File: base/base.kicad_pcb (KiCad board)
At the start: 2 copper layers, 100 x 100 mm, 108 parts, among them J1 Screw_Terminal_01x02, J2 Out, Q1 MSB92W, Q2 MJD31C, Q3 IPD50R3K0CE, Q4 MJD31C, Q5 MMBTA42, Q6 MMBTA42, Q7 MMBTA42, Q8 MMBTA42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

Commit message: Backup
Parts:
- D2: footprint Diode_THT:D_DO-41_SOD81_P10.16mm_Horizontal -> Diode_SMD:D_SMB
- moved C12 20.3 mm to (137.0, 112.0), turned to 180 degrees
- moved C20 13.7 mm to (144.9, 112.0), turned to 180 degrees
- moved R27 10.4 mm to (65.3, 121.9), turned to 45 degrees
- moved R26 8.75 mm to (68.0, 118.9), turned to 45 degrees
- moved C6 8.56 mm to (67.3, 123.9), turned to 225 degrees
- moved C18 7.86 mm to (70.3, 116.9), turned to 315 degrees
- moved D8 7.61 mm to (86.1, 99.8), turned to 90 degrees
- moved C16 6.87 mm to (69.3, 125.9), turned to 225 degrees
- moved R23 6.77 mm to (127.0, 120.5), turned to 245 degrees
- moved Q5 6.66 mm to (81.8, 99.6), turned to 180 degrees
- moved U3 6.56 mm to (70.3, 121.3), turned to 45 degrees
- moved R31 6.51 mm to (87.9, 104.4), turned to 180 degrees
- moved D9 6.49 mm to (88.4, 107.9), turned to 180 degrees
- moved C7 5.66 mm to (73.3, 118.5), turned to 45 degrees
- moved C19 5.43 mm to (71.4, 127.9), turned to 45 degrees
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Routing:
- net Net-(C17-Pad1): track 0.00 -> 67.4 mm
- net GND: track 0.00 -> 53.6 mm
- net -HV: track 0.00 -> 35.1 mm
- net Net-(C21-Pad1): track 0.00 -> 32.1 mm, vias 0 -> 2
- net Net-(C20-Pad1): track 0.00 -> 30.5 mm
- net Net-(C22-Pad1): track 0.00 -> 26.7 mm, vias 0 -> 2
- net Net-(C23-Pad1): track 0.00 -> 25.6 mm, vias 0 -> 2
- net Net-(PMT1-Pad13): track 0.00 -> 22.0 mm
- net Net-(C24-Pad1): track 0.00 -> 21.0 mm, vias 0 -> 1
- net Net-(D11-Pad1): track 0.00 -> 18.9 mm
- net Net-(D4-Pad1): track 0.00 -> 18.4 mm
- net Net-(L1-Pad1): track 0.00 -> 17.9 mm
- net Net-(PMT1-Pad6): track 0.00 -> 17.7 mm
- net Net-(Q4-Pad1): track 0.00 -> 13.4 mm
- net Net-(C25-Pad1): track 0.00 -> 13.3 mm
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
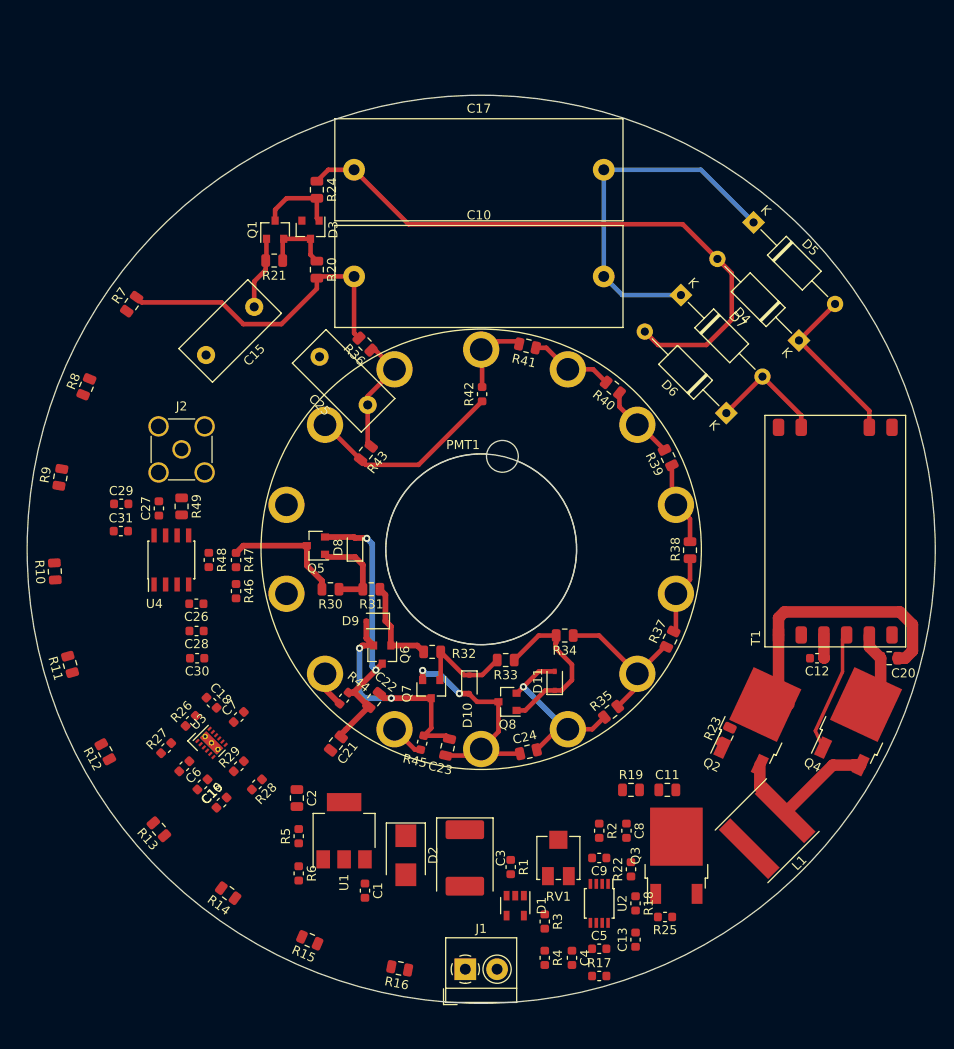
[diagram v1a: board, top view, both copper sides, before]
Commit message: Added optional G23736 (electronic goldmine) footprint
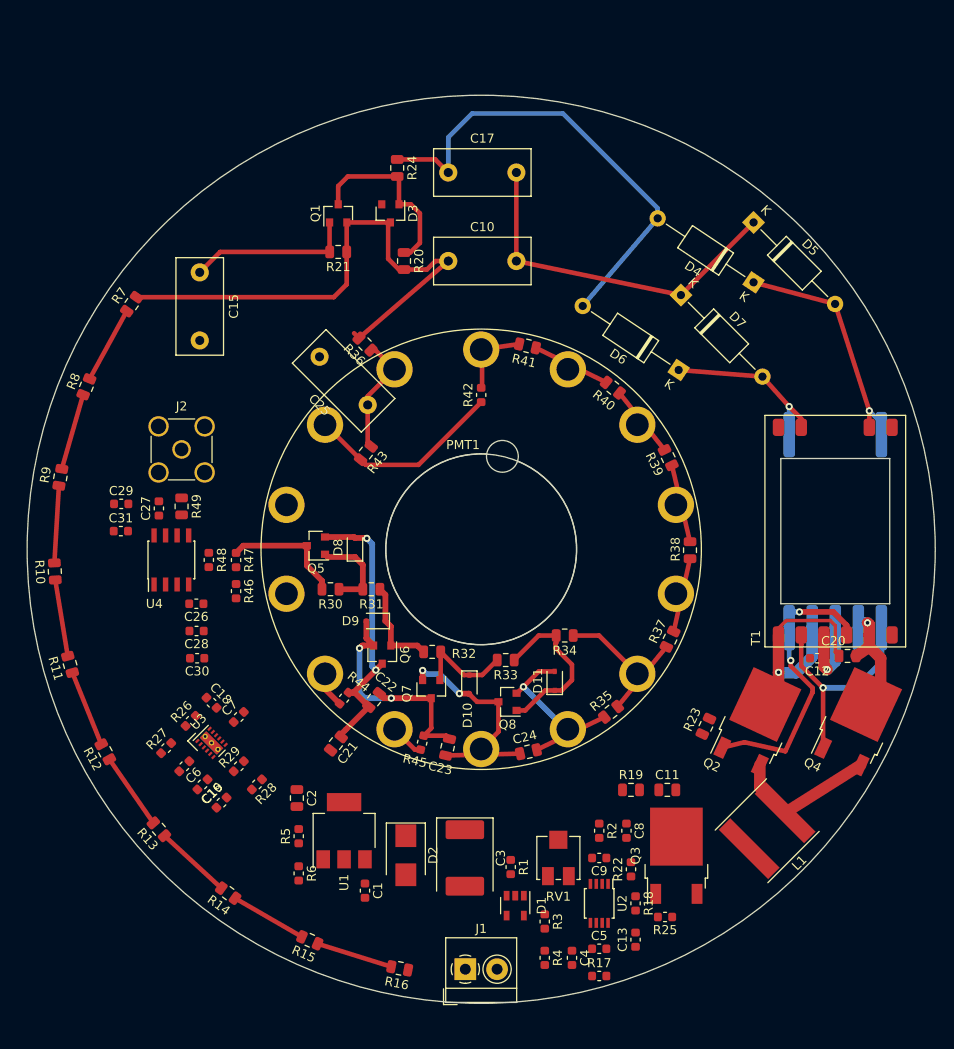
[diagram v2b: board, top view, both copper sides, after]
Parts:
- added TT1: FL2015-3LB, FL2015-3LB:G23736, F.Cu at (139.0, 98.0)
- C10: value 15n -> 10n; footprint Capacitor_THT:C_Rect_L31.5mm_W11.0mm_P27.50mm_MKS4 -> Capacitor_THT:C_Disc_D10.5mm_W5.0mm_P7.50mm
- C17: value 33n -> 10n; footprint Capacitor_THT:C_Rect_L31.5mm_W11.0mm_P27.50mm_MKS4 -> Capacitor_THT:C_Disc_D10.5mm_W5.0mm_P7.50mm
- R20: value 10k -> 0
- moved C10 10.5 mm to (96.4, 68.2)
- moved C17 10.4 mm to (96.4, 58.5)
- moved R20 9.65 mm to (91.5, 68.2)
- moved R24 9.17 mm to (90.8, 58.0)
- moved D3 8.98 mm to (90.0, 63.0)
- moved D4 8.12 mm to (130.0, 70.6), turned to 146.3 degrees
- moved Q1 7.18 mm to (84.2, 63.0)
- moved R21 7.11 mm to (84.2, 67.2)
- moved C15 7.10 mm to (69.0, 69.5), turned to 270 degrees
- moved D6 7.08 mm to (121.8, 80.2), turned to 146.3 degrees
- moved C20 4.59 mm to (140.3, 111.8), turned to 0 degrees
- moved R23 2.46 mm to (124.8, 119.5)
- moved R42 0.13 mm to (100.0, 83.0)
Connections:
- D3 pad 1: Net-(D3-Pad1) -> -HV
- Q1 pad 2: Net-(D3-Pad1) -> -HV
- R20 pad 1: Net-(D3-Pad1) -> Net-(D3-Pad2)
- R21 pad 1: Net-(D3-Pad1) -> -HV
- T1 pad 2: Net-(Q2-Pad1) -> Net-(Q4-Pad1)
- T1 pad 4: Net-(Q4-Pad1) -> Net-(Q2-Pad1)
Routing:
- net Net-(Q2-Pad1): track 0.00 -> 32.8 mm, vias 0 -> 2
- net -HV: track 35.1 -> 60.7 mm
- net Net-(C17-Pad1): track 67.4 -> 52.4 mm
- net Net-(Q4-Pad1): track 13.4 -> 24.8 mm, vias 0 -> 1
- net Net-(D3-Pad2): track 8.89 -> 20.2 mm
- net Net-(C15-Pad1): track 8.06 -> 18.5 mm
- net Net-(R13-Pad1): track 0.00 -> 8.51 mm
- net Net-(R15-Pad1): track 0.00 -> 8.51 mm
- net Net-(R8-Pad2): track 0.00 -> 8.51 mm
- net Net-(R11-Pad1): track 0.00 -> 8.51 mm
- net Net-(R10-Pad1): track 0.00 -> 8.51 mm
- net Net-(R12-Pad2): track 0.00 -> 8.51 mm
- net Net-(R10-Pad2): track 0.00 -> 8.51 mm
- net Net-(R7-Pad1): track 0.00 -> 8.51 mm
- net Net-(R14-Pad2): track 0.00 -> 8.51 mm
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
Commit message: More routing. Removed excessive ripper remover
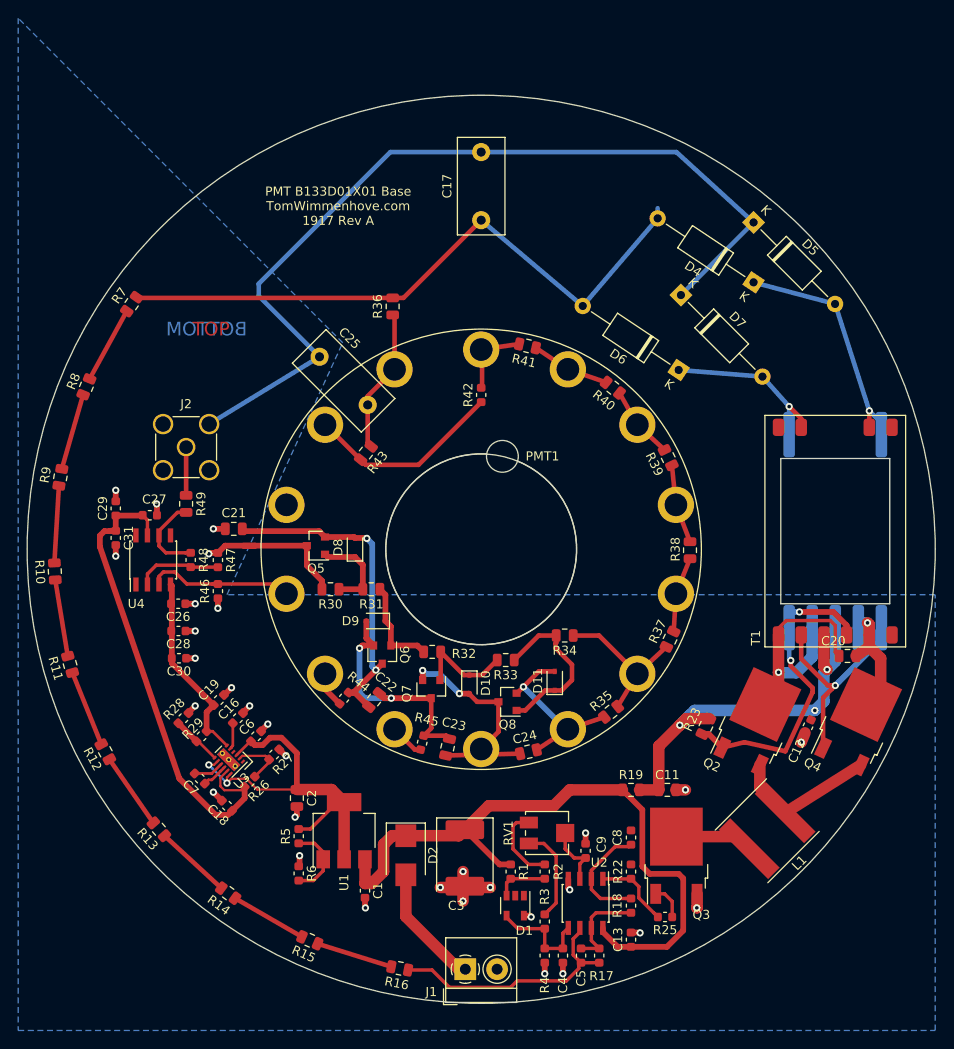
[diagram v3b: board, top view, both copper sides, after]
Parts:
- removed C10, C15: 10n, Capacitor_THT:C_Disc_D10.5mm_W5.0mm_P7.50mm
- removed D3: BZX84C47, Diode_SMD:D_SOT-23_ANK
- removed Q1: MSB92W, Package_TO_SOT_SMD:SOT-23
- removed R20: 0, Resistor_SMD:R_0805_2012Metric
- removed R21: 10M, Resistor_SMD:R_0805_2012Metric
- removed R24: 10k, Resistor_SMD:R_0805_2012Metric
- U2: footprint Package_SO:TSSOP-8_3x3mm_P0.65mm -> Package_SO:SOIC-8_3.9x4.9mm_P1.27mm
- moved C21 26.2 mm to (72.8, 97.8), turned to 180 degrees
- moved R27 11.9 mm to (77.2, 122.6), turned to 225 degrees
- moved C18 11.5 mm to (72.0, 128.2), turned to 135 degrees
- moved C19 11.3 mm to (71.1, 116.6), turned to 225 degrees
- moved R28 10.9 mm to (67.2, 118.6), turned to 45 degrees
- moved R26 9.33 mm to (74.5, 125.6), turned to 225 degrees
- moved C6 8.56 mm to (75.2, 120.6), turned to 45 degrees
- moved C16 8.28 mm to (73.2, 118.6), turned to 45 degrees
- moved C7 8.02 mm to (69.0, 125.2), turned to 135 degrees
- moved C12 7.57 mm to (136.0, 119.5), turned to 245 degrees
- moved R2 7.50 mm to (107.0, 135.5), turned to 90 degrees
- moved C17 6.38 mm to (100.0, 63.8), turned to 90 degrees
- moved R29 5.26 mm to (69.2, 120.6), turned to 225 degrees
- moved R36 5.15 mm to (90.2, 73.2), turned to 90 degrees
- moved RV1 3.02 mm to (107.2, 131.2), turned to 90 degrees
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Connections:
- C17 pad 1: Net-(C17-Pad1) -> -HV
- D4 pad 2: Net-(C17-Pad1) -> -HV
- D6 pad 2: Net-(C17-Pad1) -> -HV
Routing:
- net GND: track 53.2 -> 156.9 mm, vias 0 -> 31
- net +12V: track 0.00 -> 74.5 mm
- net +5V: track 0.00 -> 53.2 mm
- net Net-(C17-Pad1): track 52.4 -> 0.00 mm
- net Net-(C2-Pad1): track 0.00 -> 44.4 mm, vias 0 -> 2
- net Net-(C11-Pad1): track 8.95 -> 43.3 mm, vias 1 -> 3
- net Net-(C5-Pad1): track 0.00 -> 27.7 mm
- net -5V: track 0.00 -> 21.4 mm
- net Net-(D3-Pad2): track 20.2 -> 0.00 mm
- net Net-(C15-Pad1): track 18.5 -> 0.00 mm
- net Net-(PMT1-Pad11): track 0.00 -> 16.2 mm
- net Net-(D2-Pad2): track 0.00 -> 13.6 mm
- net Net-(C8-Pad2): track 0.00 -> 12.4 mm
- net Net-(C4-Pad1): track 0.00 -> 11.6 mm
- net Net-(R3-Pad1): track 0.00 -> 10.5 mm
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- added copper zone on B.Cu, net GND
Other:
- board text added: "BOTTOM"
- board text added: "PMT B133D01X01 Base TomWimmenhove.com 1917 Rev A"
- board text added: "TOP"

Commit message: Moved stuff around. Added isolation slots.
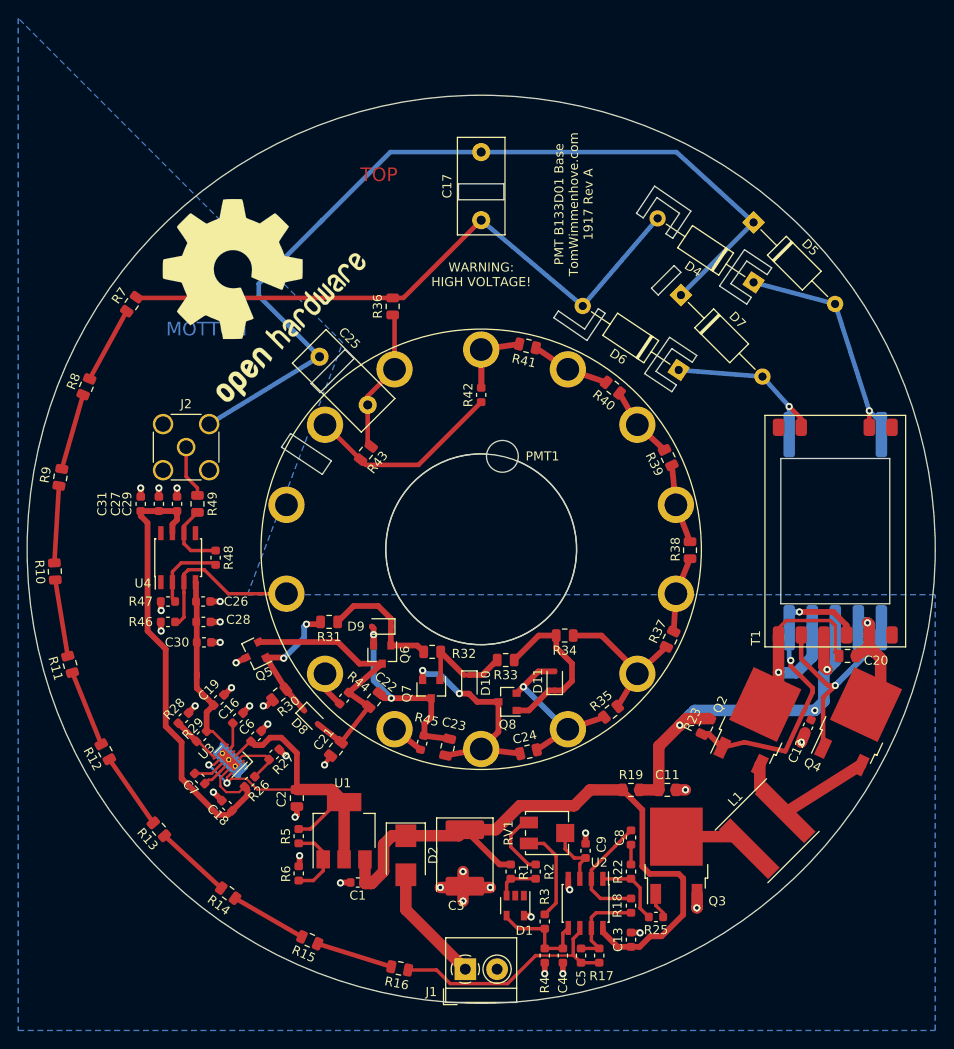
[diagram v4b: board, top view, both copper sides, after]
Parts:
- added REF**: OSHW-Logo2_24.3x20mm_SilkScreen, Symbol:OSHW-Logo2_24.3x20mm_SilkScreen, F.Cu at (73.8, 70.2)
- J2: footprint Connector_Coaxial:SMA_Amphenol_901-144_Vertical -> Connector_Coaxial:SMA_Amphenol_132291-12_Vertical
- moved C21 26.7 mm to (84.0, 122.0), turned to 231.4 degrees
- moved D8 19.3 mm to (81.2, 118.5), turned to 315 degrees
- moved Q5 13.7 mm to (75.0, 111.5), turned to 205.7 degrees
- moved R30 12.9 mm to (77.8, 116.0), turned to 218.6 degrees
- moved R47 7.15 mm to (65.5, 105.8), turned to 0 degrees
- moved C29 6.77 mm to (66.5, 95.0)
- moved R46 6.46 mm to (65.5, 108.0), turned to 0 degrees
- moved R31 5.88 mm to (83.2, 108.0)
- moved C31 4.65 mm to (62.5, 95.0), turned to 90 degrees
- moved C30 3.26 mm to (69.5, 110.2)
- moved C28 2.93 mm to (69.4, 108.0)
- moved C26 2.76 mm to (69.4, 105.8)
- moved R48 2.76 mm to (70.8, 100.9)
- moved U4 2.76 mm to (66.6, 100.9)
- moved C27 1.60 mm to (64.5, 95.0), turned to 90 degrees
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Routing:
- net Net-(C21-Pad1): track 37.0 -> 30.5 mm, vias 2 -> 0
- net Net-(D8-Pad1): track 9.96 -> 15.6 mm, vias 0 -> 2
- net Net-(C24-Pad1): track 20.4 -> 25.6 mm
- net Net-(PMT1-Pad1): track 8.26 -> 12.5 mm
- net Net-(D9-Pad1): track 10.6 -> 14.0 mm
- net GND: track 156.9 -> 154.0 mm, vias 31 -> 33
- net Net-(C8-Pad1): track 0.00 -> 2.48 mm
- net Net-(PMT1-Pad11): track 16.2 -> 18.5 mm
- net Net-(C22-Pad1): track 26.7 -> 25.0 mm
- net Net-(R2-Pad2): track 8.64 -> 7.39 mm
- net -HV: track 70.0 -> 68.9 mm
- net Net-(C5-Pad1): track 27.7 -> 26.6 mm
- net +12V: track 74.5 -> 73.5 mm
- net Net-(D1-Pad3): track 5.80 -> 4.80 mm
- net Net-(Q3-Pad1): track 3.88 -> 2.89 mm
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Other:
- outline, holes or cut-outs redrawn
- board text added: "PMT B133D01 Base TomWimmenhove.com 1917 Rev A"
- board text added: "WARNING: HIGH VOLTAGE!"
- board text removed: "PMT B133D01X01 Base TomWimmenhove.com 1917 Rev A"
